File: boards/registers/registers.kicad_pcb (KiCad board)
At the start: 2 copper layers, 100 x 100 mm, 199 parts, among them J1 ALU, J2 CU, J3 IO, J4 5V, SW1 RESET, SW2 STEP, SW3 STEP/RUN, U1 74ACT08, U10 74ACT161, U11 74ACT244, U12 74ACT244, U13 74ACT161, U14 74ACT161, U15 74ACT244, U16 74ACT244, U17 74ACT161, U18 74ACT161, U19 74ACT244, U2 74ACT244, U20 74ACT244, U21 74ACT161, U22 74ACT161, U23 74ACT244, U24 74ACT244, U25 74AC273, U26 74ACT244, U27 74ACT244, U28 74AC273, U29 74ACT244, U3 74AC273, U30 74AC20, U31 28C256, U32 62256-TSOP, U33 74ACT02, U34 74ACT14, U4 74ACT161, U5 74ACT86, U6 74ACT08, U7 74ACT32, U8 74ACT32, U9 74ACT161

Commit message: PLCC-32 socket footprint
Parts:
- U31: value 28C256 -> AT28C256-PLCC32; footprint Package_LCC:PLCC-28_SMD-Socket -> missing:PLCC-32_SMD_Socket
- moved U31 1.06 mm to (149.5, 131.5)
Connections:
- U31 pad 1: /cpu_interface/a14 -> (no net)
- U31 pad 10: /cpu_interface/a0 -> /cpu_interface/a1
- U31 pad 11: /d0 -> /cpu_interface/a0
- U31 pad 12: /d1 -> (no net)
- U31 pad 13: /d2 -> /d0
- U31 pad 14: GND -> /d1
- U31 pad 15: /d3 -> /d2
- U31 pad 16: /d4 -> GND
- U31 pad 17: /d5 -> (no net)
- U31 pad 18: /d6 -> /d3
- U31 pad 19: /d7 -> /d4
- U31 pad 2: /cpu_interface/a12 -> /cpu_interface/a14
- U31 pad 20: /cpu_interface/a15 -> /d5
- U31 pad 21: /cpu_interface/a10 -> /d6
- U31 pad 22: /~oe -> /d7
- U31 pad 23: /cpu_interface/a11 -> /cpu_interface/a15
- U31 pad 24: /cpu_interface/a9 -> /cpu_interface/a10
- U31 pad 25: /cpu_interface/a8 -> /~oe
- U31 pad 26: /cpu_interface/a13 -> (no net)
- U31 pad 27: VCC -> /cpu_interface/a11
- U31 pad 28: VCC -> /cpu_interface/a9
- U31 pad 3: /cpu_interface/a7 -> /cpu_interface/a12
- U31 pad 4: /cpu_interface/a6 -> /cpu_interface/a7
- U31 pad 5: /cpu_interface/a5 -> /cpu_interface/a6
- U31 pad 6: /cpu_interface/a4 -> /cpu_interface/a5
- U31 pad 7: /cpu_interface/a3 -> /cpu_interface/a4
- U31 pad 8: /cpu_interface/a2 -> /cpu_interface/a3
- U31 pad 9: /cpu_interface/a1 -> /cpu_interface/a2
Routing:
- net /cpu_interface/a12: track 96.8 -> 80.5 mm
- net /~oe: track 86.9 -> 103.2 mm, vias 4 -> 5
- net /cpu_interface/a15: track 93.6 -> 84.7 mm, vias 5 -> 3
- net /cpu_interface/a13: track 91.1 -> 83.2 mm, vias 3 -> 5
- net /cpu_interface/a11: track 85.8 -> 80.3 mm, vias 3 -> 5
- net /cpu_interface/a6: track 96.5 -> 91.8 mm
- net /cpu_interface/a7: track 100.9 -> 96.3 mm
- net /cpu_interface/a4: track 96.9 -> 93.4 mm
- net /cpu_interface/a14: track 91.0 -> 87.7 mm, vias 3 -> 5
- net /cpu_interface/a5: track 98.2 -> 95.3 mm
- net /cpu_interface/a1: track 84.8 -> 82.0 mm
- net /cpu_interface/a2: track 79.6 -> 76.8 mm
- net /d5: track 111.8 -> 114.0 mm
- net /d3: track 118.4 -> 120.4 mm
- net /d4: track 116.2 -> 118.2 mm
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
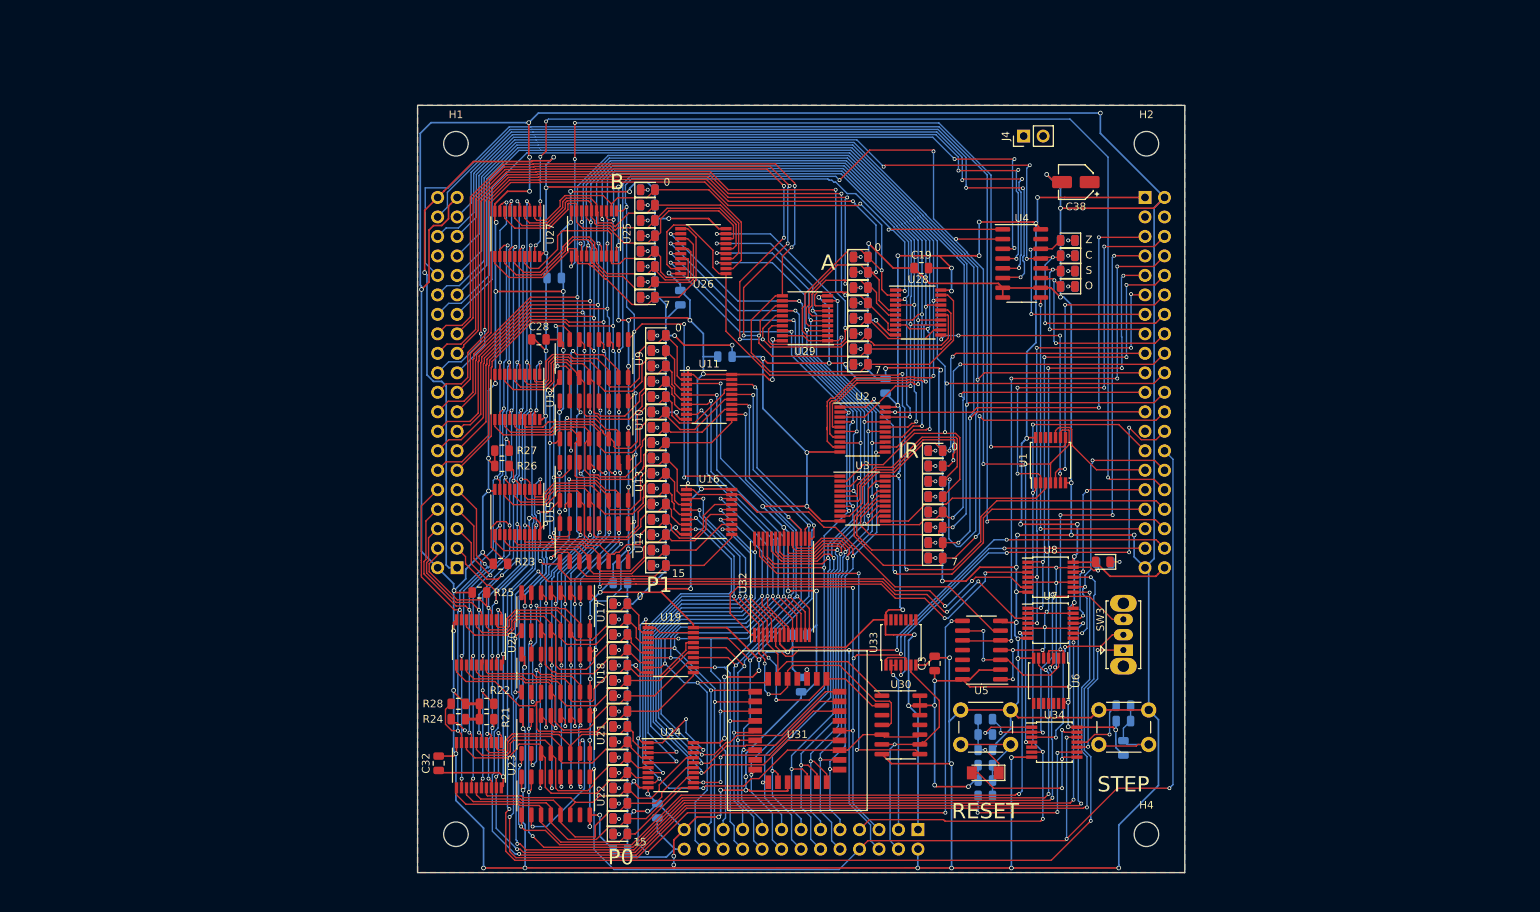
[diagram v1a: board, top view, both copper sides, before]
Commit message: Remove RAM and ROM from the registers board, board rework in progress
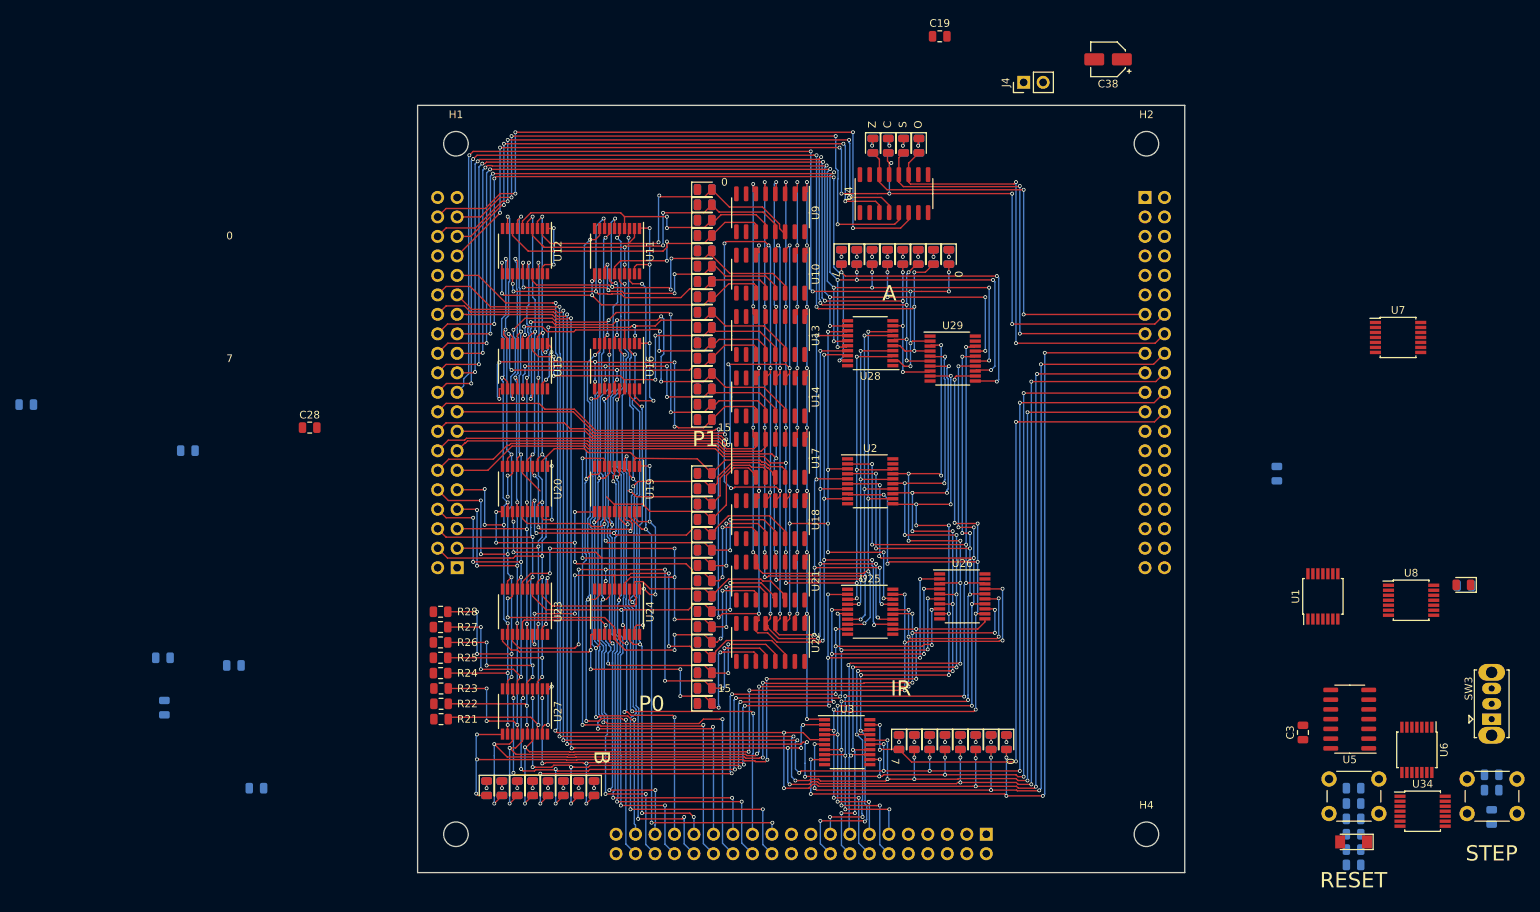
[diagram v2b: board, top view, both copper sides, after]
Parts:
- removed C30, C31, C32: 0.1u, Capacitor_SMD:C_0805_2012Metric
- removed J3: IO, Connector_PinSocket_2.54mm:PinSocket_2x13_P2.54mm_Horizontal
- removed U30: 74AC20, Package_SO:SOIC-14_3.9x8.7mm_P1.27mm
- removed U31: AT28C256-PLCC32, missing:PLCC-32_SMD_Socket
- removed U32: 62256-TSOP, Package_SO:TSOP-I-28_11.8x8mm_P0.55mm
- removed U33: 74ACT02, Package_SO:TSSOP-14_4.4x5mm_P0.65mm
- added J5: CU, Connector_PinSocket_2.54mm:PinSocket_2x20_P2.54mm_Horizontal, B.Cu at (174.1, 145.0)
- moved C26 83.1 mm to (67.0, 128.5)
- moved C6 83.1 mm to (66.8, 122.0)
- moved D46 78.3 mm to (123.0, 139.0), turned to 270 degrees
- moved R126 78.3 mm to (123.0, 139.0), turned to 270 degrees
- moved D47 76.5 mm to (121.0, 139.0), turned to 270 degrees
- moved R127 76.5 mm to (121.0, 139.0), turned to 270 degrees
- moved D48 74.8 mm to (119.0, 139.0), turned to 270 degrees
- moved R128 74.8 mm to (119.0, 139.0), turned to 270 degrees
- moved D49 73.2 mm to (117.0, 139.0), turned to 270 degrees
- moved R129 73.2 mm to (117.0, 139.0), turned to 270 degrees
- moved D50 71.6 mm to (115.0, 139.0), turned to 270 degrees
- moved R130 71.6 mm to (115.0, 139.0), turned to 270 degrees
- moved C18 71.1 mm to (70.1, 95.0)
- moved C11 70.8 mm to (49.0, 89.0)
- moved D51 70.1 mm to (113.0, 139.0), turned to 270 degrees
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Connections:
- U1 pad 11: (no net) -> Net-(U1-Pad11)
- U1 pad 12: (no net) -> GND
- U1 pad 13: (no net) -> GND
- U11 pad 12: /cpu_interface/a3 -> /cpu_interface/a6
- U11 pad 13: /pointer_pair/reg_a/lo6 -> /pointer_pair/reg_a/lo5
- U11 pad 14: /cpu_interface/a2 -> /cpu_interface/a4
- U11 pad 15: /pointer_pair/reg_a/lo5 -> /pointer_pair/reg_a/lo3
- U11 pad 16: /cpu_interface/a1 -> /cpu_interface/a2
- U11 pad 17: /pointer_pair/reg_a/lo4 -> /pointer_pair/reg_a/lo1
- U11 pad 3: /cpu_interface/a4 -> /cpu_interface/a1
- U11 pad 4: /pointer_pair/reg_a/lo1 -> /pointer_pair/reg_a/lo2
- U11 pad 5: /cpu_interface/a5 -> /cpu_interface/a3
- U11 pad 6: /pointer_pair/reg_a/lo2 -> /pointer_pair/reg_a/lo4
- U11 pad 7: /cpu_interface/a6 -> /cpu_interface/a5
- U11 pad 8: /pointer_pair/reg_a/lo3 -> /pointer_pair/reg_a/lo6
- U16 pad 12: /cpu_interface/a11 -> /cpu_interface/a14
- U16 pad 13: /pointer_pair/reg_a/hi6 -> /pointer_pair/reg_a/hi5
- U16 pad 14: /cpu_interface/a10 -> /cpu_interface/a12
- U16 pad 15: /pointer_pair/reg_a/hi5 -> /pointer_pair/reg_a/hi3
- U16 pad 16: /cpu_interface/a9 -> /cpu_interface/a10
- U16 pad 17: /pointer_pair/reg_a/hi4 -> /pointer_pair/reg_a/hi1
- U16 pad 3: /cpu_interface/a12 -> /cpu_interface/a9
- U16 pad 4: /pointer_pair/reg_a/hi1 -> /pointer_pair/reg_a/hi2
- U16 pad 5: /cpu_interface/a13 -> /cpu_interface/a11
- U16 pad 6: /pointer_pair/reg_a/hi2 -> /pointer_pair/reg_a/hi4
- U16 pad 7: /cpu_interface/a14 -> /cpu_interface/a13
- U16 pad 8: /pointer_pair/reg_a/hi3 -> /pointer_pair/reg_a/hi6
- U19 pad 12: /cpu_interface/a3 -> /cpu_interface/a6
- U19 pad 13: /pointer_pair/reg_b/lo6 -> /pointer_pair/reg_b/lo5
- U19 pad 14: /cpu_interface/a2 -> /cpu_interface/a4
- U19 pad 15: /pointer_pair/reg_b/lo5 -> /pointer_pair/reg_b/lo3
- U19 pad 16: /cpu_interface/a1 -> /cpu_interface/a2
- U19 pad 17: /pointer_pair/reg_b/lo4 -> /pointer_pair/reg_b/lo1
- U19 pad 3: /cpu_interface/a4 -> /cpu_interface/a1
- U19 pad 4: /pointer_pair/reg_b/lo1 -> /pointer_pair/reg_b/lo2
- U19 pad 5: /cpu_interface/a5 -> /cpu_interface/a3
- U19 pad 6: /pointer_pair/reg_b/lo2 -> /pointer_pair/reg_b/lo4
- U19 pad 7: /cpu_interface/a6 -> /cpu_interface/a5
- U19 pad 8: /pointer_pair/reg_b/lo3 -> /pointer_pair/reg_b/lo6
- U24 pad 12: /cpu_interface/a11 -> /cpu_interface/a14
- U24 pad 13: /pointer_pair/reg_b/hi6 -> /pointer_pair/reg_b/hi5
- U24 pad 14: /cpu_interface/a10 -> /cpu_interface/a12
- U24 pad 15: /pointer_pair/reg_b/hi5 -> /pointer_pair/reg_b/hi3
- U24 pad 16: /cpu_interface/a9 -> /cpu_interface/a10
- U24 pad 17: /pointer_pair/reg_b/hi4 -> /pointer_pair/reg_b/hi1
- U24 pad 3: /cpu_interface/a12 -> /cpu_interface/a9
- U24 pad 4: /pointer_pair/reg_b/hi1 -> /pointer_pair/reg_b/hi2
- U24 pad 5: /cpu_interface/a13 -> /cpu_interface/a11
- U24 pad 6: /pointer_pair/reg_b/hi2 -> /pointer_pair/reg_b/hi4
- U24 pad 7: /cpu_interface/a14 -> /cpu_interface/a13
- U24 pad 8: /pointer_pair/reg_b/hi3 -> /pointer_pair/reg_b/hi6
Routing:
- net GND: track 1206.6 -> 0.00 mm, vias 79 -> 0
- net VCC: track 754.1 -> 0.00 mm, vias 62 -> 0
- net /~rst: track 352.1 -> 84.0 mm, vias 16 -> 9
- net /pointer_pair/reg_a/cnt: track 177.9 -> 0.00 mm, vias 7 -> 0
- net /pointer_pair/reg_a/~oe_dl: track 182.9 -> 8.10 mm, vias 5 -> 2
- net /~clk: track 241.8 -> 68.0 mm, vias 14 -> 8
- net /~oe_alu: track 160.1 -> 0.00 mm, vias 1 -> 0
- net /pointer_pair/reg_a/~oe_dh: track 162.4 -> 6.61 mm, vias 5 -> 2
- net /~oe_b_alu: track 144.7 -> 7.66 mm, vias 5 -> 2
- net /pointer_pair/reg_b/cnt: track 128.3 -> 0.00 mm, vias 7 -> 0
- net /pointer_pair/reg_b/~oe_dl: track 138.0 -> 9.79 mm, vias 5 -> 2
- net /b_w_clk: track 123.5 -> 0.00 mm, vias 4 -> 0
- net /~oe_b_d: track 116.6 -> 0.00 mm, vias 2 -> 0
- net /pointer_pair/reg_b/~oe_dh: track 115.9 -> 9.11 mm, vias 5 -> 2
- net /~oe: track 103.2 -> 0.00 mm, vias 5 -> 0
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- removed copper zone on B.Cu, net GND
- removed copper zone on F.Cu, net VCC

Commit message: Main board revision 2
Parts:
- C10, C11, C18, C26, C34, C36, C37, C4, R167, R168, R169, R170, R171: moved to F.Cu
- moved C10 118.4 mm to (170.4, 63.8), turned to 180 degrees
- moved C26 109.1 mm to (170.9, 95.2), turned to 180 degrees
- moved C37 107.6 mm to (183.6, 117.5), turned to 180 degrees
- moved C6 93.6 mm to (160.4, 123.1), turned to 90 degrees
- moved C11 81.1 mm to (120.5, 127.4)
- moved U6 81.0 mm to (162.2, 90.0)
- moved U8 67.2 mm to (182.2, 66.8), turned to 90 degrees
- moved C3 65.4 mm to (155.1, 106.4), turned to 0 degrees
- moved R29 61.9 mm to (175.0, 105.0), turned to 270 degrees
- moved D13 61.8 mm to (175.0, 105.0), turned to 90 degrees
- moved C18 59.4 mm to (129.3, 91.0), turned to 180 degrees
- moved U5 54.9 mm to (177.2, 97.5), turned to 0 degrees
- moved R167 52.5 mm to (188.5, 133.0), turned to 180 degrees
- moved C36 52.2 mm to (188.5, 131.0)
- moved R170 51.6 mm to (189.4, 127.1), turned to 270 degrees
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- renumbered H4 to He
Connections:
- U5 pad 11: (no net) -> Net-(U5-Pad11)
- U5 pad 12: (no net) -> GND
- U5 pad 13: (no net) -> GND
- U6 pad 10: (no net) -> GND
- U6 pad 11: (no net) -> Net-(U6-Pad11)
- U6 pad 12: (no net) -> GND
- U6 pad 13: (no net) -> GND
- U6 pad 8: (no net) -> Net-(U6-Pad8)
- U6 pad 9: (no net) -> GND
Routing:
- net VCC: track 0.00 -> 439.8 mm, vias 0 -> 35
- net GND: track 0.00 -> 326.6 mm, vias 0 -> 59
- net /~oe_alu: track 0.00 -> 174.8 mm, vias 0 -> 5
- net /pointer_pair/reg_b/~oe_dh: track 9.11 -> 157.3 mm, vias 2 -> 7
- net /~rst: track 84.0 -> 223.6 mm, vias 9 -> 16
- net /~oe_b_alu: track 7.66 -> 137.3 mm, vias 2 -> 8
- net /pointer_pair/reg_b/~oe_dl: track 9.79 -> 139.1 mm, vias 2 -> 6
- net /pointer_pair/reg_b/~we_l: track 0.00 -> 126.3 mm, vias 0 -> 5
- net /pointer_pair/reg_a/~oe_dh: track 6.61 -> 115.6 mm, vias 2 -> 5
- net /~clk: track 68.0 -> 174.9 mm, vias 8 -> 13
- net /pointer_pair/reg_b/~we_h: track 0.00 -> 106.2 mm, vias 0 -> 7
- net /pointer_pair/reg_a/~we_h: track 0.00 -> 105.1 mm, vias 0 -> 5
- net /pointer_pair/~b_oe_addr: track 30.7 -> 127.2 mm, vias 5 -> 12
- net /p_selector: track 0.00 -> 93.1 mm, vias 0 -> 9
- net /pointer_pair/~a_oe_addr: track 32.0 -> 124.7 mm, vias 4 -> 11
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- added copper zone on B.Cu, net GND
- added copper zone on F.Cu, net VCC

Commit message: Fix path
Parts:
- renumbered He to H4
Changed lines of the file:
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@@
     (tags "mounting hole 3.2mm no annular m3 din965")
     (attr virtual)
-    (fp_text reference He (at 0 -3.8) (layer F.SilkS) hide
+    (fp_text reference H4 (at 0 -3.8) (layer F.SilkS) hide
       (effects (font (size 1 1) (thickness 0.15)))
     )

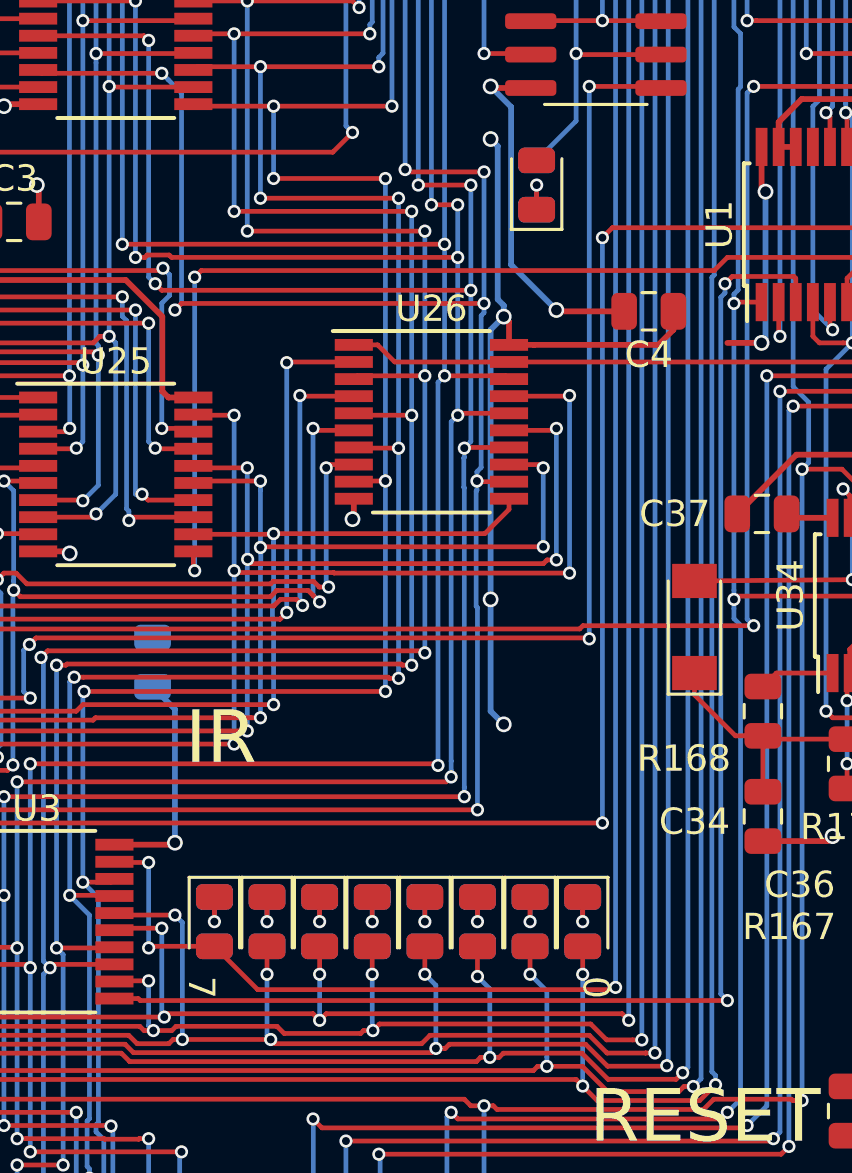
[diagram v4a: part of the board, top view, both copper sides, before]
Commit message: LEDs and LED resistors
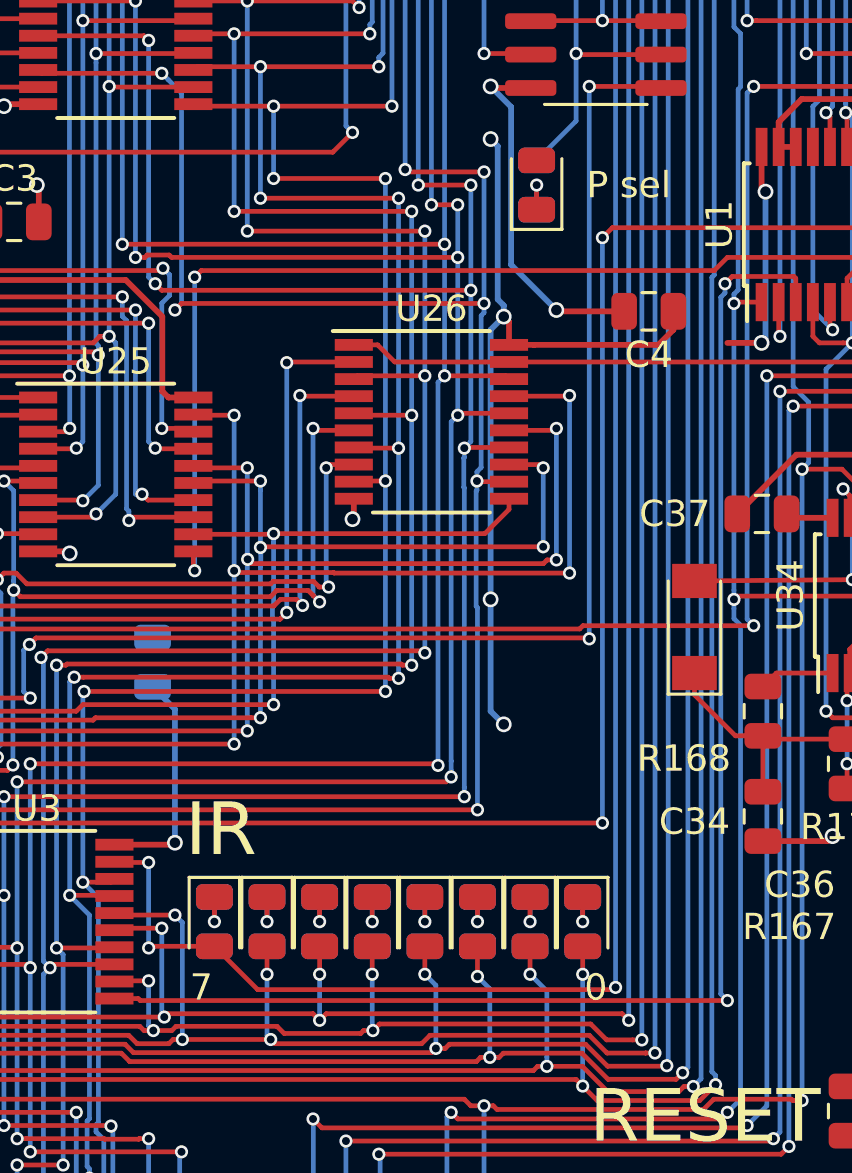
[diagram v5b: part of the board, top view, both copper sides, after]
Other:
- board text added: "P sel"
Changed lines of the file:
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@@
   (general
     (thickness 1.6)
-    (drawings 27)
+    (drawings 28)
     (tracks 5700)
     (zones 0)
@@
     )
   )
+  (gr_text "P sel" (at 178.5 105) (layer F.SilkS)
+    (effects (font (size 1 1) (thickness 0.15)))
+  )
   (dimension 12 (width 0.15) (layer Cmts.User)
     (gr_text "12.000 mm" (at 212.8 56 90) (layer Cmts.User)
@@
     (effects (font (size 2 2) (thickness 0.3)))
   )
-  (gr_text IR (at 163 126) (layer F.SilkS)
+  (gr_text IR (at 163 129.5) (layer F.SilkS)
     (effects (font (size 2 2) (thickness 0.3)))
   )
-  (gr_text 7 (at 162.25 135.5 270) (layer F.SilkS)
+  (gr_text 7 (at 162.25 135.5) (layer F.SilkS)
     (effects (font (size 1 1) (thickness 0.15)))
   )
-  (gr_text 0 (at 177.25 135.5 270) (layer F.SilkS)
+  (gr_text 0 (at 177.25 135.5) (layer F.SilkS)
     (effects (font (size 1 1) (thickness 0.15)))
   )

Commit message: Part names
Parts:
- D1, D10, D11, D12, D13, D2, D3, D4, D46, D47, D48, D49, D5, D50, D51, D52, D53, D54, D55, D56, D57, D58, D59, D6, D60, D61, D7, D8, D9: value LED -> KP-2012EC
- D14, D15, D16, D17, D18, D19, D20, D21, D22, D23, D24, D25, D26, D27, D28, D29, D30, D31, D32, D33, D34, D35, D36, D37, D38, D39, D40, D41, D42, D43, D44, D45: value LED0805 -> KP-2012EC
- R10, R11, R118, R119, R12, R120, R121, R122, R123, R124, R125, R126, R127, R128, R129, R13, R130, R131, R132, R133, R14, R15, R150, R151, R152, R153, R154, R155, R156, R157, R16, R17, R18, R19, R20, R29, R30, R31, R32, R33, R34, R35, R36, R37, R70, R71, R72, R73, R74, R75, R76, R77, R78, R79, R80, R81, R82, R83, R84, R85, R9: value LED -> 620
- SW3: value STEP/RUN -> OS102011MS2QN1
- U1, U6: value 74ACT08 -> SN74ACT08PW
- U10, U13, U14, U17, U18, U21, U22, U4, U9: value 74ACT161 -> MC74ACT161DG
- U11, U12, U15, U16, U19, U2, U20, U23, U24, U26, U27, U29: value 74ACT244 -> SN74ACT244PW
- U25, U28, U3: value 74AC273 -> MC74AC273DTR2G
- U34: value 74ACT14 -> 74ACT14MTCX
- U5: value 74ACT86 -> MC74ACT86DG
- U7, U8: value 74ACT32 -> SN74ACT32PWR

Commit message: Update net lists and PCBs with new part names
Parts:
- J1: value ALU -> SSW-120-02-G-D-RA
- J2, J5: value CU -> SSW-120-02-G-D-RA
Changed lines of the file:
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@@
       (effects (font (size 1 1) (thickness 0.15)) (justify mirror))
     )
-    (fp_text value CU (at -5.65 -51.03) (layer B.Fab)
+    (fp_text value SSW-120-02-G-D-RA (at -5.65 -51.03) (layer B.Fab)
       (effects (font (size 1 1) (thickness 0.15)) (justify mirror))
     )
@@
       (effects (font (size 1 1) (thickness 0.15)) (justify mirror))
     )
-    (fp_text value ALU (at -5.65 -51.03) (layer B.Fab)
+    (fp_text value SSW-120-02-G-D-RA (at -5.65 -51.03) (layer B.Fab)
       (effects (font (size 1 1) (thickness 0.15)) (justify mirror))
     )
@@
       (effects (font (size 1 1) (thickness 0.15)) (justify mirror))
     )
-    (fp_text value CU (at -5.65 -51.03 90) (layer B.Fab)
+    (fp_text value SSW-120-02-G-D-RA (at -5.65 -51.03 90) (layer B.Fab)
       (effects (font (size 1 1) (thickness 0.15)) (justify mirror))
     )
